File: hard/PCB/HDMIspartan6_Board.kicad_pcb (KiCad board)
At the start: 2 copper layers, 56.1 x 97.3 mm, 142 parts, among them IC1 W9812G6KH, P1 CONN_02X20, P2 CONN_02X03, U1 XC6SLX9-2TQG144C, U2 TPS62133RGTR, U3 ZLDO1117G33TA, U4 ZLDO1117G12TA, U5 MAX5864

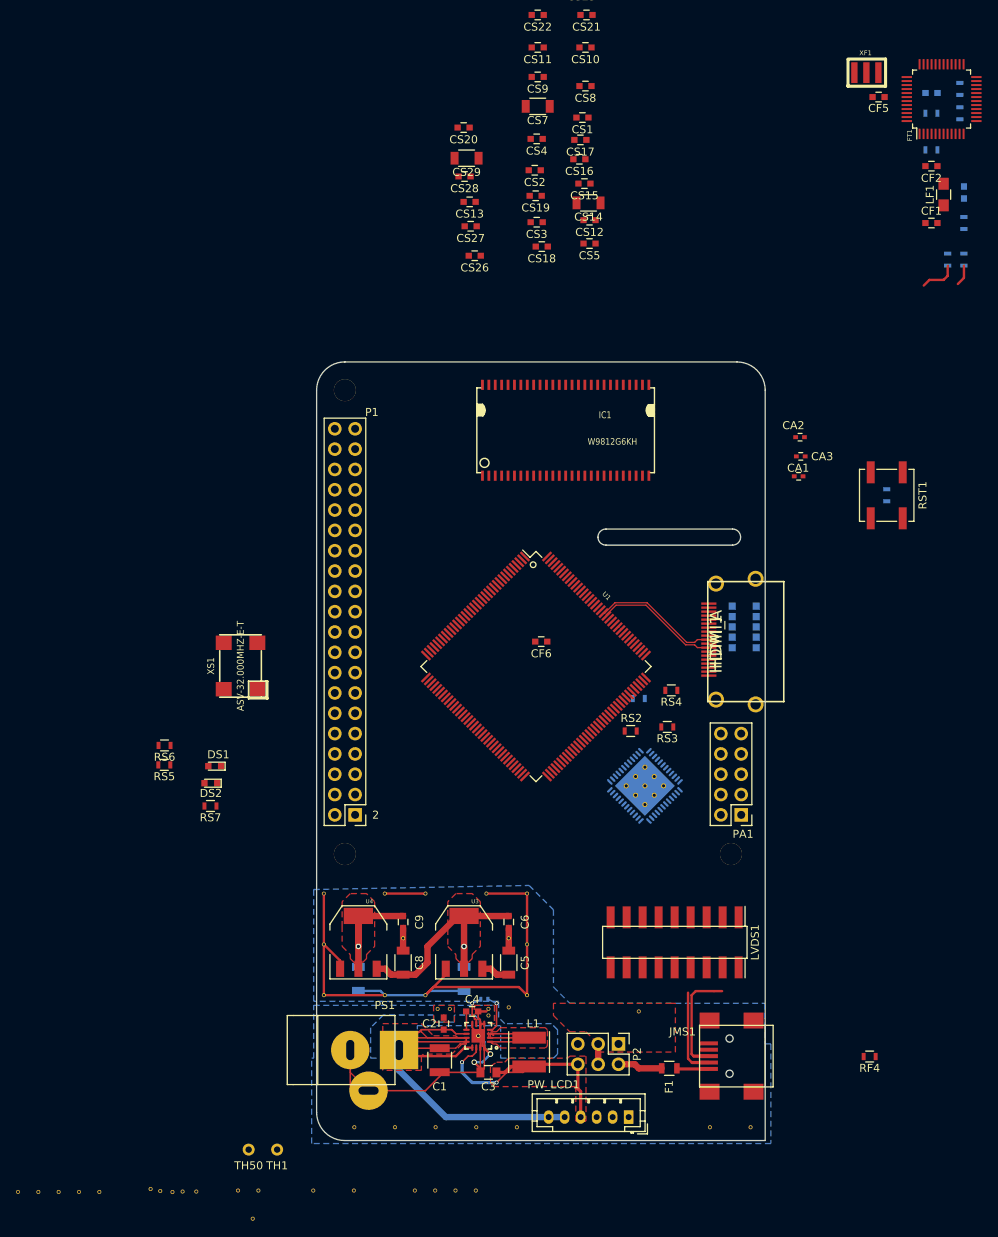
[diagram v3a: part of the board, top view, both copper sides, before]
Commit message: ok lvds  and hdmi
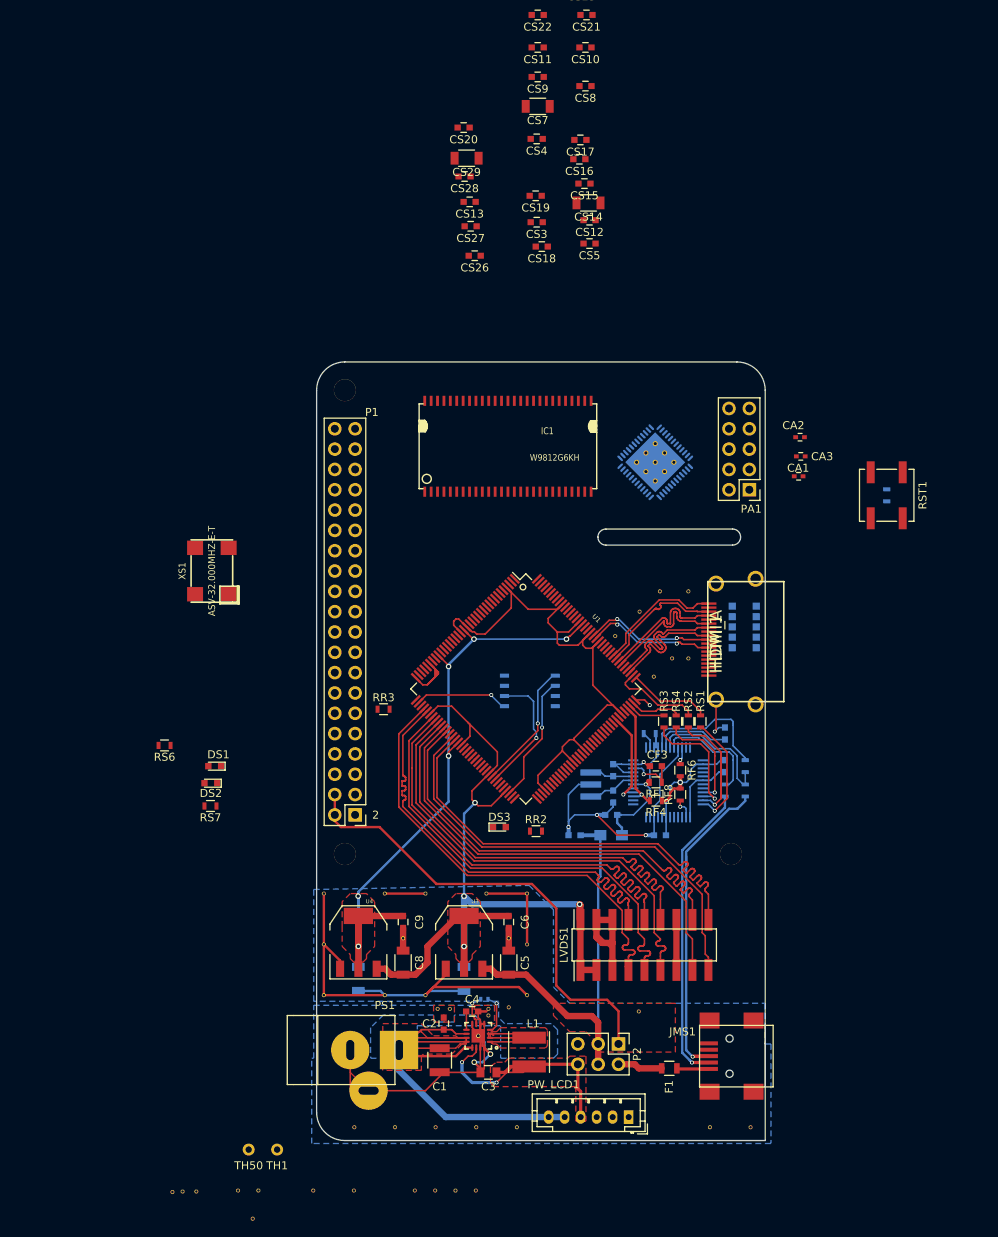
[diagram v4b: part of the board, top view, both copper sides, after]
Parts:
- removed RS5: 4.7k, Resistors_SMD:R_0603
- added DS3: LED, LEDs:LED_0603, F.Cu at (131.2, 117.8)
- added RR2: 47k, Resistors_SMD:R_0603, F.Cu at (135.7, 118.3)
- added RR3: 47k, Resistors_SMD:R_0603, F.Cu at (116.7, 103.1)
- added U6: S25FL064LABMFI013, SMD_Packages:SOIC-8-N, B.Cu at (135.0, 100.8)
- CF1, CF2, CF5, CF6, CS1, CS2, FT1, LF1, XF1: moved to B.Cu
- CF3, RF1, RF6, RF8, RS1: moved to F.Cu
- moved TH36 110.6 mm to (154.8, 88.4)
- moved TH32 106.2 mm to (151.2, 88.4)
- moved TH35 105.5 mm to (152.7, 96.7)
- moved TH37 100.9 mm to (148.7, 90.9)
- moved XF1 95.4 mm to (142.6, 112.5), turned to 270 degrees
- moved RF8 94.9 mm to (153.8, 113.8), turned to 90 degrees
- moved TH31 94.8 mm to (145.6, 93.9)
- moved TH49 93.8 mm to (154.8, 96.7)
- moved CF5 93.5 mm to (145.4, 114.0), turned to 90 degrees
- moved FT1 92.0 mm to (152.2, 112.2), turned to 270 degrees
- moved CF3 90.9 mm to (150.7, 110.2), turned to 180 degrees
- moved RF1 90.4 mm to (150.7, 112.2), turned to 180 degrees
- moved CF2 90.4 mm to (145.1, 116.3)
- moved LF1 90.2 mm to (145.1, 118.8), turned to 0 degrees
- moved TH48 89.8 mm to (150.5, 99.0)
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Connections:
- IC1 pad 10: /spartan6/DQ5 -> (no net)
- IC1 pad 11: /spartan6/DQ6 -> (no net)
- IC1 pad 13: /spartan6/DQ7 -> (no net)
- IC1 pad 15: /spartan6/DQML -> (no net)
- IC1 pad 16: /spartan6/~WE -> (no net)
- IC1 pad 17: /spartan6/~CAS -> (no net)
- IC1 pad 18: /spartan6/~RAS -> (no net)
- IC1 pad 19: /spartan6/~CS -> (no net)
- IC1 pad 2: /spartan6/DQ0 -> (no net)
- IC1 pad 20: /spartan6/BA0 -> (no net)
- IC1 pad 21: /spartan6/BA1 -> (no net)
- IC1 pad 22: /spartan6/A10 -> (no net)
- IC1 pad 23: /spartan6/A0 -> (no net)
- IC1 pad 24: /spartan6/A1 -> (no net)
- IC1 pad 25: /spartan6/A2 -> (no net)
- IC1 pad 26: /spartan6/A3 -> (no net)
- IC1 pad 29: /spartan6/A4 -> (no net)
- IC1 pad 30: /spartan6/A5 -> (no net)
- IC1 pad 31: /spartan6/A6 -> (no net)
- IC1 pad 32: /spartan6/A7 -> (no net)
- IC1 pad 33: /spartan6/A8 -> (no net)
- IC1 pad 34: /spartan6/A9 -> (no net)
- IC1 pad 35: /spartan6/A11 -> (no net)
- IC1 pad 37: /spartan6/CKE -> (no net)
- IC1 pad 38: /spartan6/CLK -> (no net)
- IC1 pad 39: /spartan6/DQMH -> (no net)
- IC1 pad 4: /spartan6/DQ1 -> (no net)
- IC1 pad 42: /spartan6/DQ8 -> (no net)
- IC1 pad 44: /spartan6/DQ9 -> (no net)
- IC1 pad 45: /spartan6/DQ10 -> (no net)
- IC1 pad 47: /spartan6/DQ11 -> (no net)
- IC1 pad 48: /spartan6/DQ12 -> (no net)
- IC1 pad 5: /spartan6/DQ2 -> (no net)
- IC1 pad 50: /spartan6/DQ13 -> (no net)
- IC1 pad 51: /spartan6/DQ14 -> (no net)
- IC1 pad 53: /spartan6/DQ15 -> (no net)
- IC1 pad 7: /spartan6/DQ3 -> (no net)
- IC1 pad 8: /spartan6/DQ4 -> (no net)
- LVDS1 pad 10: /spartan6/CH2P -> /spartan6/CH2_P
- LVDS1 pad 11: /spartan6/CH3N -> /spartan6/CH3_N
- LVDS1 pad 12: /spartan6/CH3P -> /spartan6/CH3_P
- LVDS1 pad 15: /spartan6/CLKN -> /spartan6/CLK_N
- LVDS1 pad 16: /spartan6/CLKP -> /spartan6/CLK_P
- LVDS1 pad 17: /spartan6/CH4N -> /spartan6/CH4_N
- LVDS1 pad 18: /spartan6/CH4P -> /spartan6/CH4_P
- LVDS1 pad 7: /spartan6/CH1N -> /spartan6/CH1_N
- LVDS1 pad 8: /spartan6/CH1P -> /spartan6/CH1_P
- LVDS1 pad 9: /spartan6/CH2N -> /spartan6/CH2_N
- U1 pad 1: /spartan6/~CS -> (no net)
- U1 pad 10: /spartan6/DQ1 -> (no net)
- U1 pad 11: /spartan6/DQ2 -> (no net)
- U1 pad 12: /spartan6/DQ3 -> (no net)
- U1 pad 137: /spartan6/A3 -> (no net)
- U1 pad 138: /spartan6/A2 -> (no net)
- U1 pad 139: /spartan6/A1 -> (no net)
- U1 pad 14: /spartan6/DQ4 -> (no net)
- U1 pad 140: /spartan6/A0 -> (no net)
- U1 pad 141: /spartan6/A10 -> (no net)
- U1 pad 142: /spartan6/BA1 -> (no net)
- U1 pad 143: /spartan6/BA0 -> (no net)
- U1 pad 144: +3V3 -> GND
- U1 pad 15: /spartan6/DQ5 -> (no net)
- U1 pad 16: /spartan6/DQ6 -> (no net)
- U1 pad 17: /spartan6/DQMH -> (no net)
- U1 pad 2: /spartan6/~RAS -> (no net)
- U1 pad 21: /spartan6/DQ8 -> (no net)
- U1 pad 22: /spartan6/DQ9 -> (no net)
- U1 pad 23: /spartan6/DQ10 -> (no net)
- U1 pad 24: /spartan6/DQ11 -> (no net)
- U1 pad 26: /spartan6/DQ12 -> (no net)
- U1 pad 27: /spartan6/DQ13 -> (no net)
- U1 pad 29: /spartan6/DQ14 -> (no net)
- U1 pad 30: /spartan6/DQ15 -> (no net)
- U1 pad 32: /spartan6/CLK -> (no net)
- U1 pad 33: /spartan6/CKE -> (no net)
- U1 pad 35: /spartan6/A11 -> (no net)
- U1 pad 38: Net-(RS5-Pad2) -> MEMORY_SPI_CS
- U1 pad 39: (no net) -> /spartan6/INIT_B
- U1 pad 40: /spartan6/A9 -> /spartan6/CH1_N
- U1 pad 41: /spartan6/A8 -> /spartan6/CH1_P
- U1 pad 43: /spartan6/A7 -> /spartan6/CH2_N
- U1 pad 44: /spartan6/A6 -> /spartan6/CH2_P
- U1 pad 45: /spartan6/A5 -> /spartan6/CH3_N
- U1 pad 46: /spartan6/A4 -> /spartan6/CH3_P
- U1 pad 47: (no net) -> /spartan6/CLK_N
- U1 pad 48: (no net) -> /spartan6/CLK_P
- U1 pad 5: /spartan6/~CAS -> (no net)
- U1 pad 50: /spartan6/CH1N -> /spartan6/CH4_N
- U1 pad 51: /spartan6/CH1P -> /spartan6/CH4_P
- U1 pad 55: /spartan6/CH2N -> (no net)
- U1 pad 56: /spartan6/CH2P -> (no net)
- U1 pad 57: /spartan6/CH3N -> (no net)
- U1 pad 58: /spartan6/CH3P -> (no net)
- U1 pad 6: /spartan6/~WE -> (no net)
- U1 pad 61: /spartan6/CLKN -> (no net)
- U1 pad 62: /spartan6/CLKP -> (no net)
- U1 pad 64: /spartan6/CH4N -> MEMORY_SPI_MOSI
- U1 pad 65: /spartan6/CH4P -> MEMORY_SPI_MISO
- U1 pad 7: /spartan6/DQML -> (no net)
- U1 pad 70: (no net) -> MEMORY_SPI_SCK
- U1 pad 71: (no net) -> /spartan6/DONE
- U1 pad 73: (no net) -> GND
- U1 pad 8: /spartan6/DQ7 -> (no net)
- U1 pad 9: /spartan6/DQ0 -> (no net)
- U1 pad 94: /spartan6/FPGA_CK -> (no net)
- U5 pad 6: /spartan6/FPGA_CK -> (no net)
- XS1 pad 3: /spartan6/FPGA_CK -> (no net)
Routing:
- net +3V3: track 33.0 -> 220.0 mm, vias 1 -> 5
- net GND: track 143.1 -> 226.3 mm, vias 3 -> 9
- net +1V2: track 18.6 -> 89.4 mm, vias 1 -> 6
- net /spartan6/CH2_N: track 0.00 -> 58.5 mm
- net VccRpi: track 0.00 -> 58.4 mm
- net /spartan6/CH1_N: track 0.00 -> 58.3 mm
- net /spartan6/CH3_N: track 0.00 -> 57.6 mm
- net /spartan6/CH4_N: track 0.00 -> 57.6 mm
- net /spartan6/CLK_N: track 0.00 -> 57.5 mm
- net /spartan6/CH1_P: track 0.00 -> 57.3 mm
- net /spartan6/CH4_P: track 0.00 -> 57.2 mm
- net /spartan6/CH3_P: track 0.00 -> 57.1 mm
- net /spartan6/CH2_P: track 0.00 -> 57.1 mm
- net /spartan6/CLK_P: track 0.00 -> 57.1 mm
- net +5V: track 6.15 -> 51.2 mm
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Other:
- net class Default: clearance 0.15 -> 0.18
- rule trace_clearance: 0.15 -> 0.18
- rule trace_min: 0.09 -> 0.1

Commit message: Changes in HDMISpartan6_Board
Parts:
- removed CS1, CS10, CS11, CS12, CS15, CS16, CS17, CS18, CS19, CS2, CS20, CS21, CS22, CS23, CS24, CS25, CS26, CS27, CS3, CS4, CS5, CS8, CS9: 0.1uF, Capacitors_SMD:C_0603
- removed CS13, CS28, CS6: 1uF, Capacitors_SMD:C_0603
- removed CS14, CS29, CS7: 4.7uF, Capacitors_SMD:C_1206
- removed IC1: W9812G6KH, Project:TSOPII54_SDRAM_MT48
- added C11: 4.7uF, Capacitors_SMD:C_0805, B.Cu at (130.9, 96.0)
- added C12: 4.7uF, Capacitors_SMD:C_0805, B.Cu at (124.5, 101.1)
- added C13: 4.7uF, Capacitors_SMD:C_0805, B.Cu at (128.4, 103.6)
- added C14: 4.7uF, Capacitors_SMD:C_0805, B.Cu at (141.1, 106.1)
- added C15: 4.7uF, Capacitors_SMD:C_0805, B.Cu at (138.5, 93.4)
- added C16: 4.7uF, Capacitors_SMD:C_0805, B.Cu at (128.4, 106.1)
- added C17: 4.7uF, Capacitors_SMD:C_0805, B.Cu at (141.1, 103.6)
- added C18: 0.47uF, Capacitors_SMD:C_0402, B.Cu at (138.5, 96.0)
- added C19: 4.7uF, Capacitors_SMD:C_0805, F.Cu at (122.0, 93.4)
- added C20: 4.7uF, Capacitors_SMD:C_0805, B.Cu at (124.5, 108.7)
- added C21: 4.7uF, Capacitors_SMD:C_0805, F.Cu at (143.6, 89.6)
- added C22: 0.47uF, Capacitors_SMD:C_0402, F.Cu at (124.5, 92.2)
- added C23: 4.7uF, Capacitors_SMD:C_0805, B.Cu at (141.1, 98.5)
- added C24: 0.47uF, Capacitors_SMD:C_0402, B.Cu at (141.1, 96.0)
- added C25: 0.47uF, Capacitors_SMD:C_0402, B.Cu at (136.0, 90.9)
- added C26: 4.7uF, Capacitors_SMD:C_0805, B.Cu at (144.9, 101.1)
- added C27: 0.47uF, Capacitors_SMD:C_0402, B.Cu at (138.5, 109.9)
- added C28: 0.47uF, Capacitors_SMD:C_0402, B.Cu at (136.0, 112.5)
- added C29: 4.7uF, Capacitors_SMD:C_0805, B.Cu at (130.9, 109.9)
- added C30: 0.47uF, Capacitors_SMD:C_0402, B.Cu at (130.9, 107.4)
- added C31: 0.47uF, Capacitors_SMD:C_0402, B.Cu at (124.5, 103.6)
- added C32: 4.7uF, Capacitors_SMD:C_0805, B.Cu at (130.9, 93.4)
- added C33: 0.47uF, Capacitors_SMD:C_0402, B.Cu at (133.4, 90.9)
- added C34: 0.47uF, Capacitors_SMD:C_0402, B.Cu at (124.5, 98.5)
- added C35: 0.47uF, Capacitors_SMD:C_0402, B.Cu at (153.8, 118.8)
- added C36: 4.7uF, Capacitors_SMD:C_0805, B.Cu at (150.7, 118.8)
- added C37: 0.47uF, Capacitors_SMD:C_0402, B.Cu at (141.1, 101.1)
- added C38: 4.7uF, Capacitors_SMD:C_0805, B.Cu at (128.4, 98.5)
- added C39: 0.47uF, Capacitors_SMD:C_0402, F.Cu at (143.6, 88.4)
- added C40: 0.47uF, Capacitors_SMD:C_0402, F.Cu at (124.5, 109.9)
- added C41: 0.47uF, Capacitors_SMD:C_0402, B.Cu at (137.2, 107.4)
- added C42: 0.1uF, Capacitors_SMD:C_0603, B.Cu at (159.3, 110.2)
- added C43: 4.7uF, Capacitors_SMD:C_0805, F.Cu at (96.6, 74.4)
- added C44: 1uF, Capacitors_SMD:C_0402, F.Cu at (100.0, 79.7)
- added C45: 10nF, Capacitors_SMD:C_0603, B.Cu at (122.0, 66.8)
- added C46: 10uF, Capacitors_SMD:C_0603, B.Cu at (122.0, 70.6)
- added C47: 1uF, Capacitors_SMD:C_0402, B.Cu at (122.6, 75.7)
- added C48: 1uF, Capacitors_SMD:C_0402, B.Cu at (122.6, 73.1)
- added C49: 1uF, Capacitors_SMD:C_0402, B.Cu at (122.6, 74.4)
- added C50: 4.7uF, Capacitors_SMD:C_0805, B.Cu at (156.3, 71.8)
- added C51: 4.7uF, Capacitors_SMD:C_0805, B.Cu at (153.8, 69.3)
- added C52: 4.7uF, Capacitors_SMD:C_0805, B.Cu at (156.3, 76.9)
- added C53: 0.47uF, Capacitors_SMD:C_0402, F.Cu at (156.3, 71.8)
- added C54: 0.47uF, Capacitors_SMD:C_0402, F.Cu at (153.8, 68.0)
- added C55: 0.47uF, Capacitors_SMD:C_0402, F.Cu at (156.3, 76.9)
- added C56: 4.7uF, Capacitors_SMD:C_0805, B.Cu at (146.1, 69.3)
- added C57: 0.47uF, Capacitors_SMD:C_0402, F.Cu at (146.1, 69.3)
- added CF7: 47pF, Capacitors_SMD:C_0603, B.Cu at (126.5, 82.0)
- added CF8: 47pF, Capacitors_SMD:C_0603, B.Cu at (123.3, 82.0)
- added JMS2: USB-MINI, Project:USB_Mini-B, F.Cu at (135.7, 63.2)
- added L2: HZ0805D152R-10, Resistors_SMD:R_0805_HandSoldering, B.Cu at (122.0, 68.7)
- added P3: CONN_01X03, Pin_Headers:Pin_Header_Straight_1x03_Pitch2.54mm, F.Cu at (79.6, 73.5)
- added P4: CONN_01X06, Pin_Headers:Pin_Header_Straight_1x06_Pitch2.54mm, F.Cu at (137.4, 167.1)
- added P5, P6: CONN_01X08, Pin_Headers:Pin_Header_Straight_1x08_Pitch2.54mm, F.Cu at (137.4, 167.1)
- added P7: CONN_01X10, Pin_Headers:Pin_Header_Straight_1x10_Pitch2.54mm, F.Cu at (137.4, 167.1)
- added PA2: CONN_02X05, Pin_Headers:Pin_Header_Straight_2x05_Pitch2.54mm, F.Cu at (116.9, 64.1)
- added R10: 0, Resistors_SMD:R_0603, F.Cu at (125.8, 85.8)
- added R11: 0, Resistors_SMD:R_0603, B.Cu at (116.7, 99.1)
- added R12: 0, Resistors_SMD:R_0603, F.Cu at (122.1, 85.8)
- added R13: 0, Resistors_SMD:R_0603, B.Cu at (116.7, 96.4)
- added R2: 0, Resistors_SMD:R_0603, F.Cu at (120.7, 85.8)
- added R3: 0, Resistors_SMD:R_0603, B.Cu at (116.7, 95.0)
- added R4: 0, Resistors_SMD:R_0603, F.Cu at (119.3, 85.8)
- added R5: 0, Resistors_SMD:R_0603, B.Cu at (116.7, 93.6)
- added R6: 0, Resistors_SMD:R_0603, F.Cu at (117.9, 85.8)
- added R7: 0, Resistors_SMD:R_0603, B.Cu at (116.7, 92.2)
- added R8: 0, Resistors_SMD:R_0603, F.Cu at (134.7, 74.4)
- added R9: 0, Resistors_SMD:R_0603, B.Cu at (116.7, 97.8)
- added RF10: 27R, Resistors_SMD:R_0603, F.Cu at (134.7, 70.6)
- added RF9: 27R, Resistors_SMD:R_0603, F.Cu at (134.7, 69.2)
- added RM1: 10k, Resistors_SMD:R_0603, F.Cu at (124.4, 85.8)
- added TH51: CONN_1, Project:1Pin_12mil_VIA, F.Cu at (158.8, 83.3)
- added TH52: CONN_1, Project:1Pin_12mil_VIA, F.Cu at (136.0, 84.5)
- added TH53: CONN_1, Project:1Pin_12mil_VIA, F.Cu at (93.8, 83.3)
- added TH54, TH55, TH56, TH57, TH58, TH59, TH60, TH61, TH62, TH63, TH64, TH65, TH66, TH67, TH68, TH69, TH70, TH71, TH72, TH73, TH74, TH75, TH76, TH77, TH78, TH79, TH80, TH81, TH82, TH83, TH84, TH85, TH86, TH87, TH88, TH89, TH90: CONN_1, Project:1Pin_12mil_VIA, F.Cu at (93.4, 85.8)
- added U7: ATMEGA32U4-A, Housings_QFP:LQFP-44_10x10mm_Pitch0.8mm, F.Cu at (125.4, 76.9)
- added XF2: CSTCR8M0G53Z-R0, Project:CSTCE8M00G55-RO, B.Cu at (125.8, 79.5)
- added XS2: uSD CARD, Project:Conn_uSDcard, B.Cu at (189.3, 133.3)
- CF5, CF6: value 47pF -> 15pF
- RR1: value 47k -> 4.7k
- RR2: value 47k -> 330
- RR3: value 47k -> 4.7k; moved to B.Cu
- RST1: footprint Buttons_Switches_SMD:SW_SPST_B3SL-1002P -> Buttons_Switches_SMD:SW_SPST_KMR2
- TH50: footprint Measurement_Points:Measurement_Point_Round-TH_Small -> Project:1Pin_12mil_VIA
- U5: moved to F.Cu
- XS1: moved to B.Cu
- moved TH2 108.5 mm to (166.5, 80.7)
- moved TH46 103.8 mm to (156.3, 83.3)
- moved TH45 101.4 mm to (153.8, 83.3)
- moved TH44 94.6 mm to (143.6, 83.3)
- moved TH12 88.4 mm to (143.6, 85.8)
- moved TH15 86.8 mm to (142.3, 88.4)
- moved TH50 81.7 mm to (146.1, 90.9)
- moved RS6 81.2 mm to (166.5, 132.8)
- moved TH11 76.7 mm to (162.6, 104.9)
- moved RS7 74.2 mm to (166.5, 135.3)
- moved TH34 72.1 mm to (162.6, 116.3)
- moved DS2 70.2 mm to (161.4, 135.3)
- moved DS1 69.6 mm to (161.4, 132.8)
- moved TH13 65.6 mm to (162.6, 107.4)
- moved RR1 63.8 mm to (120.7, 101.1), turned to 180 degrees
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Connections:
- net MEMORY_SPI_CS renamed /spartan6/sCS
- net MEMORY_SPI_MISO renamed /spartan6/Din
- net MEMORY_SPI_MOSI renamed /spartan6/Dout
- net MEMORY_SPI_SCK renamed /spartan6/CCLK
- DS3 pad 1: /spartan6/DONE -> GND
- DS3 pad 2: +3V3 -> /spartan6/DONE
- P1 pad 10: (no net) -> /spartan6/RpTXD
- P1 pad 11: (no net) -> /spartan6/RpGPIO_17
- P1 pad 12: (no net) -> /spartan6/RpGPIO_18
- P1 pad 13: (no net) -> /spartan6/RpGPIO_27
- P1 pad 15: (no net) -> /spartan6/RpINIT_B
- P1 pad 16: (no net) -> /spartan6/RpGPIO_23
- P1 pad 18: (no net) -> /spartan6/RpPROG
- P1 pad 19: /ADC_DAC/SPI_MOSI -> /spartan6/RpMOSI
- P1 pad 21: (no net) -> /spartan6/RpMISO
- P1 pad 22: (no net) -> /spartan6/RpDONE
- P1 pad 23: /ADC_DAC/SPI_SCK -> /spartan6/RpSCK
- P1 pad 24: (no net) -> /spartan6/RpGPIO_08
- P1 pad 26: (no net) -> /spartan6/RpCS
- P1 pad 28: (no net) -> /spartan6/RpID_SC
- P1 pad 3: (no net) -> /spartan6/RpSDA
- P1 pad 5: (no net) -> /spartan6/RpSCL
- P1 pad 7: (no net) -> /spartan6/RpGPIO_04
- P1 pad 8: (no net) -> /spartan6/RpRXD
- RR2 pad 1: /spartan6/DONE -> +3V3
- RR2 pad 2: GND -> /spartan6/DONE
- U1 pad 1: (no net) -> /ADC_DAC/adDA6
- U1 pad 10: (no net) -> /ADC_DAC/adDA0
- U1 pad 121: (no net) -> /ADC_DAC/adCS
- U1 pad 126: (no net) -> /spartan6/FPGA_CLK
- U1 pad 127: (no net) -> /ADC_DAC/adSCK
- U1 pad 131: (no net) -> /ADC_DAC/adMOSI
- U1 pad 132: (no net) -> /ADC_DAC/adDD9
- U1 pad 133: (no net) -> /ADC_DAC/adDD8
- U1 pad 134: (no net) -> /ADC_DAC/adDD7
- U1 pad 137: (no net) -> /ADC_DAC/adDD6
- U1 pad 138: (no net) -> /ADC_DAC/adDD5
- U1 pad 139: (no net) -> /ADC_DAC/adDD4
- U1 pad 14: (no net) -> /ADC_DAC/adCLK
- U1 pad 140: (no net) -> /ADC_DAC/adDD3
- U1 pad 141: (no net) -> /ADC_DAC/adDD2
- U1 pad 142: (no net) -> /ADC_DAC/adDD1
- U1 pad 143: (no net) -> /ADC_DAC/adDD0
- U1 pad 2: (no net) -> /ADC_DAC/adDA7
- U1 pad 5: (no net) -> /ADC_DAC/adDA5
- U1 pad 6: (no net) -> /ADC_DAC/adDA4
- U1 pad 60: GND -> /spartan6/M1
- U1 pad 61: (no net) -> /spartan6/RpID_SC
- U1 pad 62: (no net) -> /spartan6/RpGPIO_08
- U1 pad 7: (no net) -> /ADC_DAC/adDA3
- U1 pad 74: (no net) -> /spartan6/RpCS
- U1 pad 75: (no net) -> /atmega32u4/uP0
- U1 pad 78: (no net) -> /spartan6/RpGPIO_23
- U1 pad 79: (no net) -> /spartan6/RpGPIO_27
- U1 pad 8: (no net) -> /ADC_DAC/adDA2
- U1 pad 80: (no net) -> /spartan6/RpGPIO_18
- U1 pad 81: (no net) -> /spartan6/RpGPIO_17
- U1 pad 82: (no net) -> /spartan6/RpTXD
- U1 pad 83: (no net) -> /spartan6/RpRXD
- U1 pad 84: (no net) -> /spartan6/RpGPIO_04
- U1 pad 85: (no net) -> /spartan6/RpSCL
- U1 pad 87: (no net) -> /spartan6/RpSDA
- U1 pad 9: (no net) -> /ADC_DAC/adDA1
- U5 pad 13: (no net) -> /ADC_DAC/adDA0
- U5 pad 14: (no net) -> /ADC_DAC/adDA1
- U5 pad 15: (no net) -> /ADC_DAC/adDA2
- U5 pad 16: (no net) -> /ADC_DAC/adDA3
- U5 pad 19: (no net) -> /ADC_DAC/adDA4
- U5 pad 20: (no net) -> /ADC_DAC/adDA5
- U5 pad 21: (no net) -> /ADC_DAC/adDA6
- U5 pad 22: (no net) -> /ADC_DAC/adDA7
- U5 pad 23: (no net) -> /ADC_DAC/adDD0
- U5 pad 24: (no net) -> /ADC_DAC/adDD1
- U5 pad 25: (no net) -> /ADC_DAC/adDD2
- U5 pad 26: (no net) -> /ADC_DAC/adDD3
- U5 pad 27: (no net) -> /ADC_DAC/adDD4
- U5 pad 28: (no net) -> /ADC_DAC/adDD5
- U5 pad 29: (no net) -> /ADC_DAC/adDD6
- U5 pad 30: (no net) -> /ADC_DAC/adDD7
- U5 pad 31: (no net) -> /ADC_DAC/adDD8
- U5 pad 32: (no net) -> /ADC_DAC/adDD9
- U5 pad 34: /ADC_DAC/SPI_MOSI -> /ADC_DAC/adMOSI
- U5 pad 35: /ADC_DAC/SPI_SCK -> /ADC_DAC/adSCK
- U5 pad 36: (no net) -> /ADC_DAC/adCS
- U5 pad 39: GND -> +3V3
- U5 pad 6: (no net) -> /ADC_DAC/adCLK
- U5 pad 7: (no net) -> GND
- XS1 pad 3: (no net) -> /spartan6/FPGA_CLK
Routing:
- net GND: track 226.3 -> 512.1 mm, vias 9 -> 48
- net +3V3: track 220.0 -> 445.9 mm, vias 5 -> 32
- net /spartan6/REBOOT: track 0.00 -> 75.5 mm, vias 0 -> 2
- net /atmega32u4/uP0: track 0.00 -> 68.5 mm, vias 0 -> 2
- net +1V2: track 89.4 -> 155.5 mm, vias 6 -> 5
- net /spartan6/RpCS: track 0.00 -> 64.9 mm, vias 0 -> 2
- net /spartan6/DONE: track 0.00 -> 63.7 mm, vias 0 -> 3
- net /spartan6/Dout: track 16.0 -> 78.7 mm, vias 1 -> 4
- net /spartan6/Din: track 15.9 -> 77.4 mm, vias 1 -> 4
- net /spartan6/CCLK: track 16.0 -> 75.3 mm, vias 1 -> 4
- net /spartan6/RpID_SC: track 0.00 -> 45.7 mm, vias 0 -> 3
- net /spartan6/RpTXD: track 0.00 -> 45.1 mm, vias 0 -> 1
- net /spartan6/RpGPIO_08: track 0.00 -> 44.9 mm, vias 0 -> 2
- net /spartan6/RpGPIO_18: track 0.00 -> 44.6 mm, vias 0 -> 1
- net /spartan6/RpGPIO_23: track 0.00 -> 44.4 mm, vias 0 -> 1
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- added copper zone on B.Cu, net +3V3
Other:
- board size 56.1 x 97.3 mm -> 58.2 x 97.3 mm
- net class Default: clearance 0.18 -> 0.2
- net class Vcc: via_dia 0.7 -> 0.5; via_drill 0.4 -> 0.3
- rule trace_clearance: 0.18 -> 0.2

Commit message: versión 1.0
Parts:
- removed the P4 at (137.4, 167.1)
- removed the P5 at (137.4, 167.1)
- removed P6: CONN_01X08, Pin_Headers:Pin_Header_Straight_1x08_Pitch2.54mm
- removed P7: CONN_01X10, Pin_Headers:Pin_Header_Straight_1x10_Pitch2.54mm
- added ?: , Project:RPi_Hat_Mounting_Hole, F.Cu at (160.8, 63.2)
- added R14: 2k2, Resistors_SMD:R_0603, B.Cu at (126.5, 90.9)
- added R15: 2k2, Resistors_SMD:R_0603, B.Cu at (128.0, 90.9)
- added TH100: CONN_1, Project:1Pin_12mil_VIA, F.Cu at (108.7, 78.2)
- added TH101: CONN_1, Project:1Pin_12mil_VIA, F.Cu at (108.7, 83.3)
- added TH102: CONN_1, Project:1Pin_12mil_VIA, F.Cu at (108.7, 93.4)
- added TH103: CONN_1, Project:1Pin_12mil_VIA, F.Cu at (108.7, 98.5)
- added TH104: CONN_1, Project:1Pin_12mil_VIA, F.Cu at (108.7, 103.6)
- added TH105: CONN_1, Project:1Pin_12mil_VIA, F.Cu at (108.7, 108.7)
- added TH106: CONN_1, Project:1Pin_12mil_VIA, F.Cu at (108.7, 113.8)
- added TH107: CONN_1, Project:1Pin_12mil_VIA, F.Cu at (108.7, 125.2)
- added TH108: CONN_1, Project:1Pin_12mil_VIA, F.Cu at (146.1, 156.3)
- added TH109: CONN_1, Project:1Pin_12mil_VIA, F.Cu at (152.5, 156.3)
- added TH110: CONN_1, Project:1Pin_12mil_VIA, F.Cu at (139.8, 156.3)
- added TH91: CONN_1, Project:1Pin_12mil_VIA, F.Cu at (122.0, 59.1)
- added TH92: CONN_1, Project:1Pin_12mil_VIA, F.Cu at (116.9, 59.1)
- added TH93: CONN_1, Project:1Pin_12mil_VIA, F.Cu at (111.8, 59.1)
- added TH94: CONN_1, Project:1Pin_12mil_VIA, F.Cu at (115.7, 66.8)
- added TH95: CONN_1, Project:1Pin_12mil_VIA, F.Cu at (129.6, 64.2)
- added TH96: CONN_1, Project:1Pin_12mil_VIA, F.Cu at (142.3, 64.2)
- added TH97: CONN_1, Project:1Pin_12mil_VIA, F.Cu at (136.0, 73.1)
- added TH98: CONN_1, Project:1Pin_12mil_VIA, F.Cu at (108.7, 68.0)
- added TH99: CONN_1, Project:1Pin_12mil_VIA, F.Cu at (108.7, 73.1)
- RR2: moved to B.Cu
- TH1: footprint Measurement_Points:Measurement_Point_Round-TH_Small -> Project:1Pin_12mil_VIA
- moved TH72 88.6 mm to (152.5, 151.9)
- moved TH66 88.4 mm to (163.9, 139.2)
- moved TH65 86.9 mm to (163.9, 136.6)
- moved TH67 86.4 mm to (161.4, 139.1)
- moved TH68 84.4 mm to (158.8, 139.1)
- moved TH70 82.2 mm to (151.2, 144.2)
- moved TH71 80.4 mm to (148.7, 144.2)
- moved TH69 78.7 mm to (151.2, 139.2)
- moved TH83 78.6 mm to (148.7, 141.7)
- moved TH73 77.2 mm to (133.4, 151.9)
- moved TH74 75.9 mm to (130.9, 151.9)
- moved TH85 75.7 mm to (165.2, 61.7)
- moved TH75 74.7 mm to (128.4, 151.9)
- moved TH84 74.6 mm to (165.2, 65.5)
- moved TH63 74.3 mm to (165.2, 104.9)
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- renumbered DS3 to LED1, DS2 to LED2, DS1 to LED3, PA1 to P4, PA2 to P5
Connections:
- LED2 pad 1: (no net) -> /spartan6/LED1
- LED3 pad 1: (no net) -> /spartan6/LED2
- P1 pad 27: (no net) -> /spartan6/RpID_SD
- P1 pad 29: (no net) -> /spartan6/RpGPIO_05
- P1 pad 31: (no net) -> /spartan6/RpGPIO_06
- P1 pad 32: (no net) -> /spartan6/RpGPIO_12
- P1 pad 33: (no net) -> /spartan6/RpGPIO_13
- P1 pad 35: (no net) -> /spartan6/RpGPIO_19
- P1 pad 36: (no net) -> /spartan6/RpGPIO_16
- P1 pad 37: (no net) -> /spartan6/RpGPIO_26
- P1 pad 38: (no net) -> /spartan6/RpGPIO_20
- P1 pad 40: (no net) -> /spartan6/RpGPIO_21
- P4 pad 1: +3V3 -> GND
- P4 pad 2: GND -> +3V3
- P4 pad 5: /ADC_DAC/ID+ -> /ADC_DAC/ID-
- P4 pad 6: /ADC_DAC/ID- -> /ADC_DAC/ID+
- P4 pad 7: /ADC_DAC/IA+ -> /ADC_DAC/IA-
- P4 pad 8: /ADC_DAC/IA- -> /ADC_DAC/IA+
- U1 pad 100: (no net) -> /spartan6/LED1
- U1 pad 12: (no net) -> /atmega32u4/uD3
- U1 pad 15: (no net) -> /atmega32u4/uD2
- U1 pad 16: (no net) -> /atmega32u4/uD1
- U1 pad 17: (no net) -> /atmega32u4/uD0
- U1 pad 21: (no net) -> /atmega32u4/rst_um
- U1 pad 24: (no net) -> /spartan6/RpGPIO_21
- U1 pad 26: (no net) -> /spartan6/RpGPIO_26
- U1 pad 27: (no net) -> /spartan6/RpGPIO_20
- U1 pad 29: (no net) -> /spartan6/RpGPIO_19
- U1 pad 30: (no net) -> /spartan6/RpGPIO_13
- U1 pad 32: (no net) -> /spartan6/RpGPIO_16
- U1 pad 33: (no net) -> /spartan6/RpGPIO_06
- U1 pad 34: (no net) -> /spartan6/RpGPIO_12
- U1 pad 35: (no net) -> /spartan6/RpGPIO_05
- U1 pad 59: (no net) -> /spartan6/RpID_SD
- U1 pad 92: (no net) -> /spartan6/usCS
- U1 pad 93: (no net) -> /spartan6/usMOSI
- U1 pad 94: (no net) -> /spartan6/usSCK
- U1 pad 95: (no net) -> /spartan6/usMISO
- U1 pad 97: (no net) -> /spartan6/usCD
- U7 pad 18: (no net) -> /atmega32u4/uD0
- U7 pad 19: (no net) -> /atmega32u4/uD1
- U7 pad 20: (no net) -> /atmega32u4/uD2
- U7 pad 21: (no net) -> /atmega32u4/uD3
- U7 pad 27: (no net) -> /spartan6/LED2
- XS2 pad 2: (no net) -> /spartan6/usCS
- XS2 pad 3: (no net) -> /spartan6/usMOSI
- XS2 pad 5: (no net) -> /spartan6/usSCK
- XS2 pad 7: (no net) -> /spartan6/usMISO
- XS2 pad 9: (no net) -> /spartan6/usCD
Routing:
- net GND: track 512.1 -> 1257.9 mm, vias 48 -> 51
- net +3V3: track 445.9 -> 541.7 mm, vias 32 -> 33
- net /spartan6/LED1: track 0.00 -> 74.7 mm, vias 0 -> 2
- net /ADC_DAC/adCLK: track 8.12 -> 49.1 mm, vias 1 -> 2
- net /spartan6/RpID_SD: track 0.00 -> 40.6 mm, vias 0 -> 3
- net /spartan6/usCS: track 0.00 -> 38.4 mm, vias 0 -> 1
- net /spartan6/usMOSI: track 0.00 -> 38.0 mm, vias 0 -> 1
- net /spartan6/usCD: track 0.00 -> 35.6 mm, vias 0 -> 1
- net /spartan6/usSCK: track 0.00 -> 35.5 mm, vias 0 -> 1
- net /spartan6/RpGPIO_21: track 0.00 -> 34.4 mm, vias 0 -> 1
- net /spartan6/usMISO: track 0.00 -> 34.3 mm, vias 0 -> 1
- net /spartan6/RpGPIO_20: track 0.00 -> 33.1 mm, vias 0 -> 1
- net /spartan6/RpGPIO_26: track 0.00 -> 30.6 mm, vias 0 -> 1
- net /spartan6/LED2: track 0.00 -> 30.6 mm, vias 0 -> 2
- net +5V: track 51.2 -> 81.6 mm
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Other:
- board size 58.2 x 97.3 mm -> 58.5 x 99 mm
